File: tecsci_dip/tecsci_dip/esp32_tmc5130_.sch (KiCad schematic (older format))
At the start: 20 parts, among them IC201 TMC5130, J201 Conn_01x19_ESP32, J202 Conn_01x19_ESP32, U201 AKL182_04_POL_HEADER, X201 Oscillator_636L3C016M00000

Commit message: add value and footprint
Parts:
- removed C210, C211: C, TMC5130-Eval_v15:C_POL_RAD_THT_5X10X12.5, symbol Device:C
- added C210, C211: 100uF, TMC5130-Eval_v15:C_POL_RAD_THT_5X10X12.5, symbol Device:CP
- C201: value C -> 10nF/16V/0603
- C202, C204, C206, C208: value C -> 100nF
- C203: value C -> 470nF
- C205, C209: value C -> 4.7uF
- C207: value C -> 22nF
- D201: value SMBJ -> SMBJ43A
- J201, J202: footprint (none) -> Connector_PinSocket_2.54mm:PinSocket_1x19_P2.54mm_Vertical
- R203: value R -> 0R
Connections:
- net GND: now also IC201.1 (TST_MODE), C210.2, C211.2
- net SDI: now also IC201.7 (SDO_NAO_CFG0); no longer IC201.5 (SDI_NAI_CFG1)
- net SDO: now also IC201.5 (SDI_NAI_CFG1); no longer IC201.7 (SDO_NAO_CFG0)
- net at C206.1, C208.1, C209.1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: now also C210.1, C211.1
- no-connect marks 42 -> 41
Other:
- note added: "A Motor PaP"
- note added: "Pin out ESP32 NODEMCU v1.1"
- note added: "Trinamic CI"
- note removed: "Shield ESP32 NODEMCU v1.1"
- moved on the sheet: C204, C206, C208, C209, D201

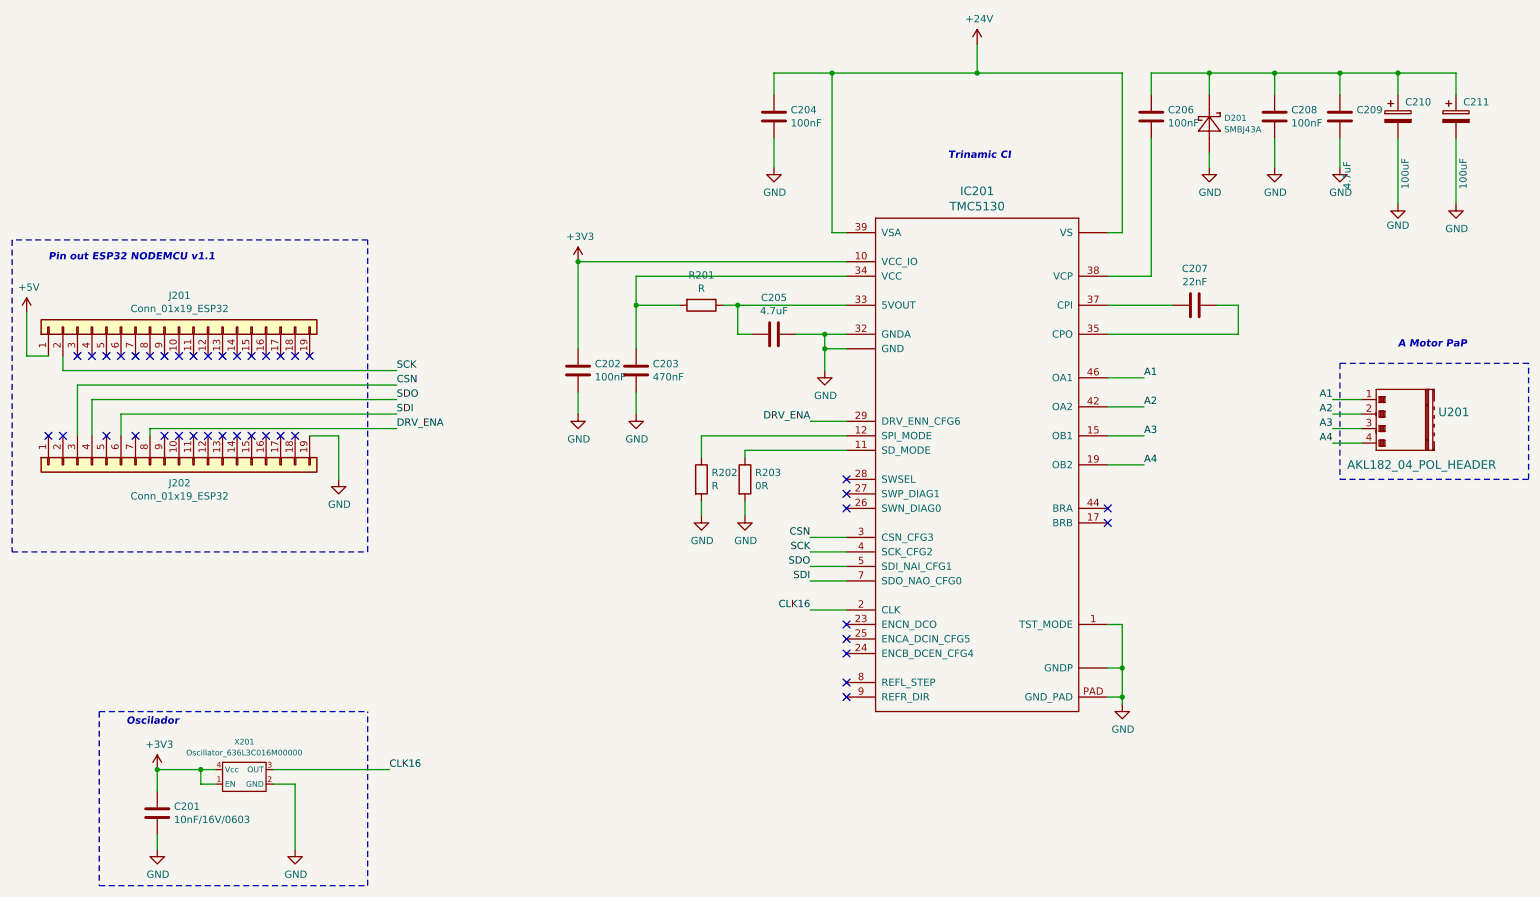
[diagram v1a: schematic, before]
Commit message: agrego valor faltantes en esquematico
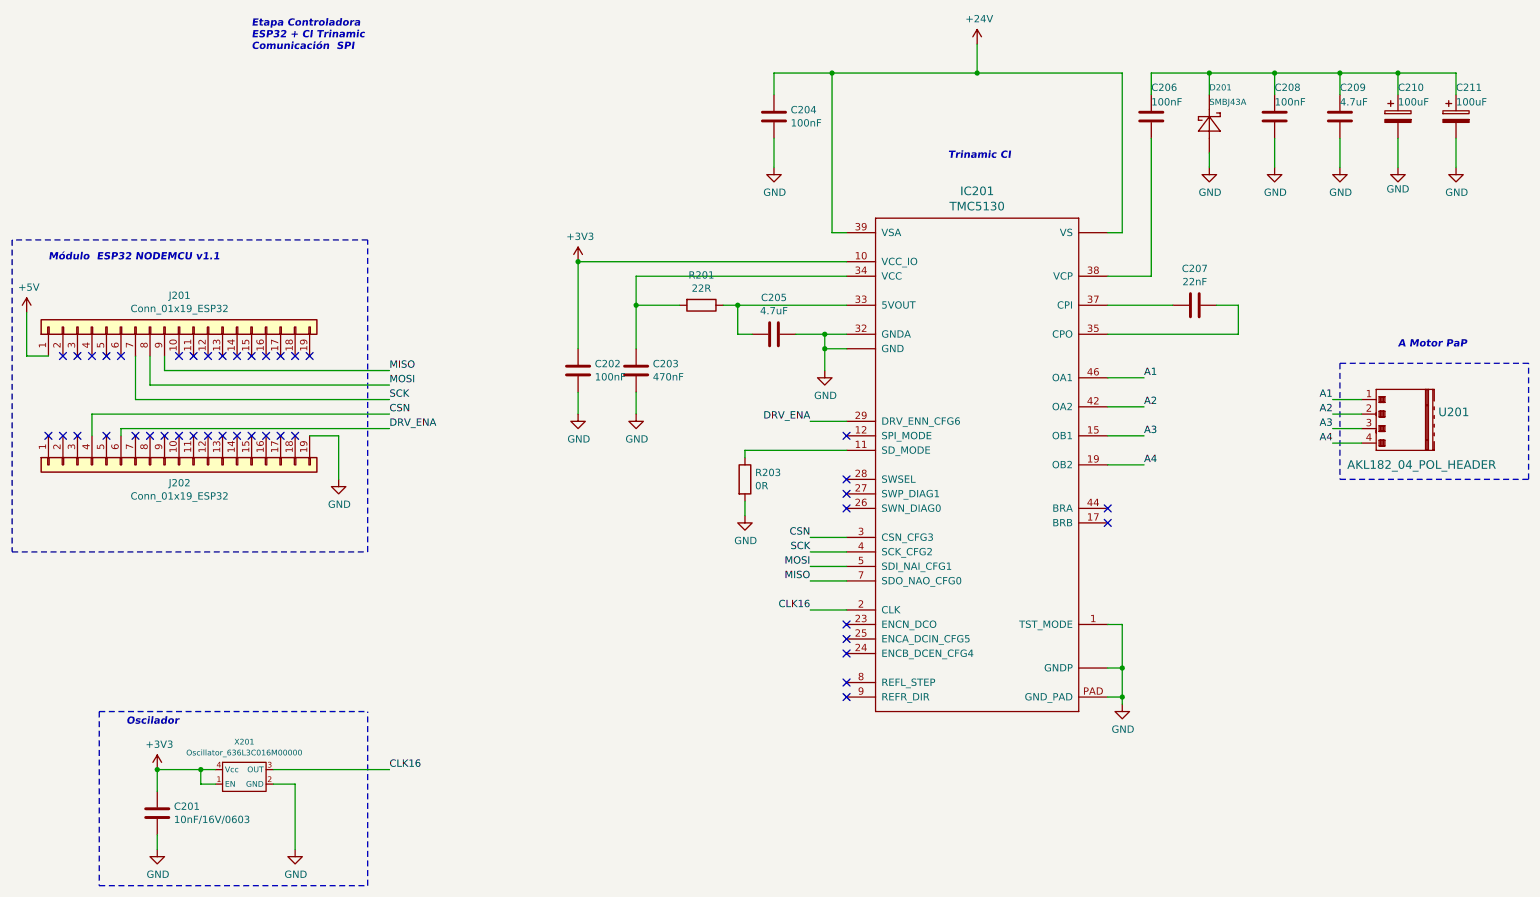
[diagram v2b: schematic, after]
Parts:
- removed R202: R, TMC5130-Eval_v15:RCL_0603, symbol Device:R
- R201: value R -> 22R
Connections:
- net CSN: now also J202.4 (Pin_4); no longer J202.3 (Pin_3)
- net DRV_ENA: now also J202.6 (Pin_6); no longer J202.8 (Pin_8)
- net SCK: now also J201.7 (Pin_7); no longer J201.2 (Pin_2)
- net MOSI: now reaches J201.8 (Pin_8)
- net MOSI: now also IC201.5 (SDI_NAI_CFG1)
- net MISO: now reaches J201.9 (Pin_9)
- net MISO: now also IC201.7 (SDO_NAO_CFG0)
- removed net SDI: IC201.7 (SDO_NAO_CFG0), J202.6 (Pin_6)
- removed net SDO: IC201.5 (SDI_NAI_CFG1), J202.4 (Pin_4)
- no-connect marks 41 -> 42
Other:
- note added: "Etapa Controladora\nESP32 + CI Trinamic \nComunicación SPI"
- note added: "Módulo ESP32 NODEMCU v1.1"
- note removed: "Pin out ESP32 NODEMCU v1.1"
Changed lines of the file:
@@
 	3100 2450 650  2450
 Text Notes 900  2600 0    50   Italic 10
-Pin out ESP32 NODEMCU v1.1
+Módulo  ESP32 NODEMCU v1.1
 $Comp
 L Device:C C204
@@
 U 1 1 5D95B59C
 P 8500 1600
-F 0 "C206" H 8615 1646 50  0000 L CNN
-F 1 "100nF" H 8615 1555 50  0000 L CNN
+F 0 "C206" H 8500 1800 50  0000 L CNN
+F 1 "100nF" H 8500 1700 50  0000 L CNN
 F 2 "TMC5130-Eval_v15:0603" H 8538 1450 50  0001 C CNN
 F 3 "~" H 8500 1600 50  0001 C CNN
@@
 U 1 1 5D95BF52
 P 9350 1600
-F 0 "C208" H 9465 1646 50  0000 L CNN
-F 1 "100nF" H 9465 1555 50  0000 L CNN
+F 0 "C208" H 9350 1800 50  0000 L CNN
+F 1 "100nF" H 9350 1700 50  0000 L CNN
 F 2 "TMC5130-Eval_v15:0603" H 9388 1450 50  0001 C CNN
 F 3 "~" H 9350 1600 50  0001 C CNN
@@
 U 1 1 5D95C3E0
 P 9800 1600
-F 0 "C209" H 9915 1646 50  0000 L CNN
-F 1 "4.7uF" V 9850 1100 50  0000 L CNN
+F 0 "C209" H 9800 1800 50  0000 L CNN
+F 1 "4.7uF" H 9800 1700 50  0000 L CNN
 F 2 "TMC5130-Eval_v15:C1210" H 9838 1450 50  0001 C CNN
 F 3 "~" H 9800 1600 50  0001 C CNN
@@
 U 1 1 5D95D43B
 P 8900 1650
-F 0 "D201" V 8940 1547 42  0000 R CNN
-F 1 "SMBJ43A" V 8861 1547 42  0000 R CNN
+F 0 "D201" V 9150 1650 42  0000 R CNN
+F 1 "SMBJ43A" V 9050 1650 42  0000 R CNN
 F 2 "TMC5130-Eval_v15:SMB" H 8900 1650 50  0001 C CNN
 F 3 "" H 8900 1650 50  0001 C CNN
@@
 $EndComp
 $Comp
-L Device:R R202
-U 1 1 5D964AE9
-P 5400 4100
-F 0 "R202" H 5470 4146 50  0000 L CNN
-F 1 "R" H 5470 4055 50  0000 L CNN
-F 2 "TMC5130-Eval_v15:RCL_0603" V 5330 4100 50  0001 C CNN
-F 3 "~" H 5400 4100 50  0001 C CNN
-	1    5400 4100
-	1    0    0    -1
-$EndComp
-$Comp
 L Device:R R203
 U 1 1 5D9650B9
@@
 P 5400 2900
 F 0 "R201" V 5193 2900 50  0000 C CNN
-F 1 "R" V 5284 2900 50  0000 C CNN
+F 1 "22R" V 5284 2900 50  0000 C CNN
 F 2 "TMC5130-Eval_v15:0603" V 5330 2900 50  0001 C CNN
 F 3 "~" H 5400 2900 50  0001 C CNN
@@
 L power:GND #PWR0219
 U 1 1 5D968302
-P 10200 2200
-F 0 "#PWR0219" H 10200 1950 50  0001 C CNN
-F 1 "GND" H 10200 2050 50  0000 C CNN
-F 2 "" H 10200 2200 50  0001 C CNN
-F 3 "" H 10200 2200 50  0001 C CNN
-	1    10200 2200
+P 10200 1950
+F 0 "#PWR0219" H 10200 1700 50  0001 C CNN
+F 1 "GND" H 10200 1800 50  0000 C CNN
+F 2 "" H 10200 1950 50  0001 C CNN
+F 3 "" H 10200 1950 50  0001 C CNN
+	1    10200 1950
 	1    0    0    -1
 $EndComp
@@
 SCK
 Text Label 6150 4700 2    50   ~ 0
-SDO
+MOSI
 Text Label 6150 4800 2    50   ~ 0
-SDI
+MISO
 Wire Wire Line
 	6150 4500 6400 4500
@@
 Wire Wire Line
 	6150 4800 6400 4800
-Text Label 3300 3450 0    50   ~ 0
+Text Label 3250 3650 0    50   ~ 0
 CSN
-Text Label 3300 3350 0    50   ~ 0
+Text Label 3250 3550 0    50   ~ 0
 SCK
-Text Label 3300 3650 0    50   ~ 0
-SDI
-Text Label 3300 3550 0    50   ~ 0
-SDO
+Text Label 3250 3350 0    50   ~ 0
+MISO
+Text Label 3250 3750 0    50   ~ 0
+DRV_ENA
 $Comp
 L power:+5V #PWR0201
@@
 Wire Wire Line
 	6150 3700 6400 3700
-Text Label 3300 3750 0    50   ~ 0
-DRV_ENA
+Text Label 3250 3450 0    50   ~ 0
+MOSI
 NoConn ~ 6400 5100
 NoConn ~ 6400 5200
@@
 Wire Wire Line
 	5700 3900 5700 3950
-Wire Wire Line
-	6400 3800 5400 3800
-Wire Wire Line
-	5400 3800 5400 3950
-$Comp
-L power:GND #PWR0209
-U 1 1 5D9D5725
-P 5400 4350
-F 0 "#PWR0209" H 5400 4100 50  0001 C CNN
-F 1 "GND" H 5405 4177 50  0000 C CNN
-F 2 "" H 5400 4350 50  0001 C CNN
-F 3 "" H 5400 4350 50  0001 C CNN
-	1    5400 4350
-	1    0    0    -1
-$EndComp
 $Comp
 L power:GND #PWR0210
@@
 	5700 4350 5700 4250
 Wire Wire Line
-	5400 4250 5400 4350
-Wire Wire Line
 	2450 6200 2600 6200
 Wire Wire Line
@@
 Wire Wire Line
 	750  3250 750  2950
-Wire Wire Line
-	1000 3250 1000 3350
-Wire Wire Line
-	1000 3350 3300 3350
-Wire Wire Line
-	1400 3800 1400 3650
-Wire Wire Line
-	1400 3650 3300 3650
-Wire Wire Line
-	3300 3550 1200 3550
-Wire Wire Line
-	1200 3550 1200 3800
-Wire Wire Line
-	3300 3450 1100 3450
-Wire Wire Line
-	1100 3450 1100 3800
-Wire Wire Line
-	1600 3800 1600 3750
-Wire Wire Line
-	1600 3750 3300 3750
 NoConn ~ 1100 3250
 NoConn ~ 1200 3250
 NoConn ~ 1300 3250
 NoConn ~ 1400 3250
-NoConn ~ 1500 3250
-NoConn ~ 1600 3250
-NoConn ~ 1700 3250
 NoConn ~ 1800 3250
 NoConn ~ 1900 3250
@@
 NoConn ~ 2200 3250
 NoConn ~ 2300 3250
-NoConn ~ 2400 3250
 NoConn ~ 2500 3250
 NoConn ~ 2600 3250
@@
 L power:GND #PWR0101
 U 1 1 5D9EEA74
-P 10600 2200
-F 0 "#PWR0101" H 10600 1950 50  0001 C CNN
-F 1 "GND" H 10605 2027 50  0000 C CNN
-F 2 "" H 10600 2200 50  0001 C CNN
-F 3 "" H 10600 2200 50  0001 C CNN
-	1    10600 2200
+P 10600 1950
+F 0 "#PWR0101" H 10600 1700 50  0001 C CNN
+F 1 "GND" H 10605 1777 50  0000 C CNN
+F 2 "" H 10600 1950 50  0001 C CNN
+F 3 "" H 10600 1950 50  0001 C CNN
+	1    10600 1950
 	1    0    0    -1
 $EndComp
@@
 U 1 1 5DA90CAF
 P 10200 1600
-F 0 "C210" H 10250 1700 50  0000 L CNN
-F 1 "100uF" V 10250 1100 50  0000 L CNN
+F 0 "C210" H 10200 1800 50  0000 L CNN
+F 1 "100uF" H 10200 1700 50  0000 L CNN
 F 2 "TMC5130-Eval_v15:C_POL_RAD_THT_5X10X12.5" H 10238 1450 50  0001 C CNN
 F 3 "~" H 10200 1600 50  0001 C CNN
@@
 U 1 1 5DA91323
 P 10600 1600
-F 0 "C211" H 10650 1700 50  0000 L CNN
-F 1 "100uF" V 10650 1100 50  0000 L CNN
+F 0 "C211" H 10600 1800 50  0000 L CNN
+F 1 "100uF" H 10600 1700 50  0000 L CNN
 F 2 "TMC5130-Eval_v15:C_POL_RAD_THT_5X10X12.5" H 10638 1450 50  0001 C CNN
 F 3 "~" H 10600 1600 50  0001 C CNN
@@
 $EndComp
 Wire Wire Line
-	10600 1750 10600 2200
-Wire Wire Line
-	10200 1750 10200 2200
+	10200 1750 10200 1950
 Wire Wire Line
 	8500 1300 8900 1300
@@
 	8300 5100 8300 5400
 Connection ~ 8300 5400
+Wire Wire Line
+	10600 1750 10600 1950
+NoConn ~ 1000 3250
+NoConn ~ 1100 3800
+Wire Wire Line
+	3250 3650 1200 3650
+Wire Wire Line
+	1200 3650 1200 3800
+Wire Wire Line
+	3250 3550 1500 3550
+Wire Wire Line
+	1500 3550 1500 3250
+Wire Wire Line
+	1600 3250 1600 3450
+Wire Wire Line
+	1600 3450 3250 3450
+Wire Wire Line
+	1700 3250 1700 3350
+Wire Wire Line
+	1700 3350 3250 3350
+Wire Wire Line
+	1400 3800 1400 3750
+Wire Wire Line
+	1400 3750 3250 3750
+NoConn ~ 1600 3800
+NoConn ~ 6400 3800
+NoConn ~ 2400 3250
+Text Notes 2300 1150 0    50   Italic 10
+Etapa Controladora\nESP32 + CI Trinamic \nComunicación  SPI
 $EndSCHEMATC

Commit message: update board
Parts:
- removed C201: 10nF/16V/0603, TMC5130-Eval_v15:0603, symbol Device:C
- removed C211: 100uF, TMC5130-Eval_v15:C_POL_RAD_THT_5X10X12.5, symbol Device:CP
- removed X201: Oscillator_636L3C016M00000, Oscillator:Oscillator_SMD_EuroQuartz_XO53-4Pin_5.0x3.2mm, symbol Ponchobrücke-cache:Oscillator_636L3C016M00000
- added C201: 100uF, Capacitor_THT:CP_Radial_D10.0mm_P7.50mm, symbol Device:CP
- added R202, R204: 0R15/0.5W, Resistor_SMD:R_1206_3216Metric, symbol Device:R
- C202, C203, C204, C205, C206, C208: footprint TMC5130-Eval_v15:0603 -> Capacitor_SMD:C_0805_2012Metric
- C207: footprint TMC5130-Eval_v15:C0603 -> Capacitor_SMD:C_0805_2012Metric
- C209: footprint TMC5130-Eval_v15:C1210 -> Capacitor_SMD:C_1210_3225Metric
- C210: footprint TMC5130-Eval_v15:C_POL_RAD_THT_5X10X12.5 -> Capacitor_THT:CP_Radial_D10.0mm_P7.50mm
- R201: value 22R -> 2R2; footprint TMC5130-Eval_v15:0603 -> Resistor_SMD:R_0805_2012Metric
- R203: footprint TMC5130-Eval_v15:RCL_0603 -> Resistor_SMD:R_0805_2012Metric
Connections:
- net +24V: now also C206.1, C208.1, C209.1, C210.1, D201.C, C201.1
- net +3V3: now also J201.19 (Pin_19)
- net DRV_ENA: now also J202.8 (Pin_8); no longer J202.6 (Pin_6)
- net GND: now also C201.2, R202.2, R204.2
- net at IC201.17 (BRB): now also R202.1
- net at IC201.44 (BRA): now also R204.1
- net +5V renamed +5VD
- net A1: no longer names the net of U201.1
- net A1: now also IC201.19 (OB2); no longer IC201.46 (OA1)
- net A2: no longer names the net of U201.2
- net A2: now also IC201.15 (OB1); no longer IC201.42 (OA2)
- net A3: no longer names the net of U201.3
- net A3: now also IC201.42 (OA2); no longer IC201.15 (OB1)
- net A4: no longer names the net of U201.4
- net A4: now also IC201.46 (OA1); no longer IC201.19 (OB2)
- net CLK16: no longer names the net of IC201.2 (CLK)
- no-connect marks 42 -> 40
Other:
- note added: "Microcontrolador ESP32 \nCI Trinamic TMC5130\nComunicación SPI"
- note removed: "Etapa Controladora\nESP32 + CI Trinamic \nComunicación SPI"
- note removed: "Oscilador"

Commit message: add correcciones compañero
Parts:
- C205: digikey# (none) -> 399-15711-2-ND; manf (none) -> KEMET; manf# (none) -> C0805C475K4RACAUTO
- IC201: digikey# (none) -> 1460-1124-ND; manf (none) -> Trinamic Motion Control GmbH; manf# (none) -> TMC5130A-TA
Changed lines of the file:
@@
 F 1 "TMC5130" H 7300 5781 59  0000 C CNN
 F 2 "TMC5130-Eval_v15:QFP50P900X900X113-49N_NOFID" H 7300 4000 50  0001 C CNN
-F 3 "" H 7300 4000 50  0001 C CNN
+F 3 "https://www.trinamic.com/_scripts/download.php?file=_articles%2Fproducts%2Fintegrated-circuits%2Ftmc5130%2F_datasheet%2FTMC5130_datasheet.pdf" H 7300 4000 50  0001 C CNN
+F 4 "1460-1124-ND " H 7300 4000 50  0001 C CNN "digikey#"
+F 5 "Trinamic Motion Control GmbH" H 7300 4000 50  0001 C CNN "manf"
+F 6 "TMC5130A-TA" H 7300 4000 50  0001 C CNN "manf#"
 	1    7300 4000
 	1    0    0    -1
@@
 F 1 "4.7uF" V 5739 3100 50  0000 C CNN
 F 2 "Capacitor_SMD:C_0805_2012Metric" H 5938 2950 50  0001 C CNN
-F 3 "~" H 5900 3100 50  0001 C CNN
+F 3 "https://api.kemet.com/component-edge/download/datasheet/C0805C475K4RACAUTO.pdf" H 5900 3100 50  0001 C CNN
+F 4 "399-15711-2-ND " H 5900 3100 50  0001 C CNN "digikey#"
+F 5 "KEMET" H 5900 3100 50  0001 C CNN "manf"
+F 6 "C0805C475K4RACAUTO" H 5900 3100 50  0001 C CNN "manf#"
 	1    5900 3100
 	0    1    1    0

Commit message: Se corrigen todos los errores marcados por el profesor, excepto pasar a footprint conectores de ESP32, ya que la v2 contendra al CI
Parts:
- D201: digikey# (none) -> SMBJ43AFSTR-ND; manf (none) -> Taiwan Semiconductor Corporation; manf# (none) -> SMBJ43A
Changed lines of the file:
@@
 Title "Dip Coater - ESP32  TMC5130"
 Date "2019-10-02"
-Rev "1"
-Comp "Tecsci"
-Comment1 "Martin Abel Gambarotta"
-Comment2 "Revisor: Mariano Campos"
-Comment3 ""
-Comment4 ""
+Rev "2"
+Comp "Tecsci  Tecnología para Ciencia                            Licensed under CERN OHL v.1.2"
+Comment1 "Ing. Electrónico  Martin Abel Gambarotta"
+Comment2 ""
+Comment3 "Revisor: Diego Brengi"
+Comment4 "Revisor: Mariano Campos"
 $EndDescr
 $Comp
@@
 F 1 "SMBJ43A" V 9050 1650 42  0000 R CNN
 F 2 "TMC5130-Eval_v15:SMB" H 8900 1650 50  0001 C CNN
-F 3 "" H 8900 1650 50  0001 C CNN
+F 3 "https://www.taiwansemi.com/products/datasheet/SMBJ%20SERIES_P1812.pdf" H 8900 1650 50  0001 C CNN
+F 4 "SMBJ43AFSTR-ND" H 8900 1650 50  0001 C CNN "digikey#"
+F 5 "Taiwan Semiconductor Corporation" H 8900 1650 50  0001 C CNN "manf"
+F 6 "SMBJ43A" H 8900 1650 50  0001 C CNN "manf#"
 	1    8900 1650
 	0    -1   -1   0
